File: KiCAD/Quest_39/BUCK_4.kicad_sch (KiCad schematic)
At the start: 21 parts

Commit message: Fixed most ERC errors
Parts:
- gave numbers to parts that had none: 21
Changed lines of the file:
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@@
   (symbol (lib_id "Device:C") (at 99.06 45.72 0) (unit 1)
     (in_bom yes) (on_board yes) (fields_autoplaced)
-    (property "Reference" "C?" (id 0) (at 102.87 44.4499 0)
+    (property "Reference" "C54" (id 0) (at 102.87 44.4499 0)
       (effects (font (size 1.27 1.27)) (justify left))
     )
@@
   (symbol (lib_id "Device:C_Polarized") (at 353.06 171.45 0) (unit 1)
     (in_bom yes) (on_board yes)
-    (property "Reference" "C?" (id 0) (at 356.8495 170.1375 0)
+    (property "Reference" "C60" (id 0) (at 356.8495 170.1375 0)
       (effects (font (size 1.27 1.27)) (justify left))
     )
@@
   (symbol (lib_id "Device:R") (at 321.31 214.63 0) (unit 1)
     (in_bom yes) (on_board yes) (fields_autoplaced)
-    (property "Reference" "R?" (id 0) (at 323.85 213.3599 0)
+    (property "Reference" "R27" (id 0) (at 323.85 213.3599 0)
       (effects (font (size 1.27 1.27)) (justify left))
     )
@@
   (symbol (lib_id "Device:C") (at 111.76 45.72 0) (unit 1)
     (in_bom yes) (on_board yes) (fields_autoplaced)
-    (property "Reference" "C?" (id 0) (at 115.57 44.4499 0)
+    (property "Reference" "C55" (id 0) (at 115.57 44.4499 0)
       (effects (font (size 1.27 1.27)) (justify left))
     )
@@
   (symbol (lib_id "Device:C_Polarized") (at 392.43 171.45 0) (unit 1)
     (in_bom yes) (on_board yes)
-    (property "Reference" "C?" (id 0) (at 396.2195 170.1375 0)
+    (property "Reference" "C63" (id 0) (at 396.2195 170.1375 0)
       (effects (font (size 1.27 1.27)) (justify left))
     )
@@
   (symbol (lib_id "MCP4151:MCP4151-502E{slash}SN") (at 252.73 219.71 0) (unit 1)
     (in_bom yes) (on_board yes)
-    (property "Reference" "U?" (id 0) (at 311.15 213.36 0)
+    (property "Reference" "U19" (id 0) (at 311.15 213.36 0)
       (effects (font (size 1.524 1.524)))
     )
@@
   (symbol (lib_id "Device:C_Polarized") (at 85.09 45.72 0) (unit 1)
     (in_bom yes) (on_board yes) (fields_autoplaced)
-    (property "Reference" "C?" (id 0) (at 88.9 43.5609 0)
+    (property "Reference" "C53" (id 0) (at 88.9 43.5609 0)
       (effects (font (size 1.27 1.27)) (justify left))
     )
@@
   (symbol (lib_id "Device:C") (at 336.55 223.52 0) (unit 1)
     (in_bom yes) (on_board yes) (fields_autoplaced)
-    (property "Reference" "C?" (id 0) (at 340.36 222.2499 0)
+    (property "Reference" "C64" (id 0) (at 340.36 222.2499 0)
       (effects (font (size 1.27 1.27)) (justify left))
     )
@@
   (symbol (lib_id "Device:C") (at 124.46 45.72 0) (unit 1)
     (in_bom yes) (on_board yes) (fields_autoplaced)
-    (property "Reference" "C?" (id 0) (at 128.27 44.4499 0)
+    (property "Reference" "C56" (id 0) (at 128.27 44.4499 0)
       (effects (font (size 1.27 1.27)) (justify left))
     )
@@
   (symbol (lib_id "Analog_ADC:INA226") (at 77.47 72.39 0) (unit 1)
     (in_bom yes) (on_board yes)
-    (property "Reference" "U?" (id 0) (at 82.55 60.96 0)
+    (property "Reference" "U17" (id 0) (at 82.55 60.96 0)
       (effects (font (size 1.27 1.27)) (justify left))
     )
@@
   (symbol (lib_id "Device:R") (at 46.99 48.26 0) (unit 1)
     (in_bom yes) (on_board yes) (fields_autoplaced)
-    (property "Reference" "R?" (id 0) (at 49.53 46.9899 0)
+    (property "Reference" "R24" (id 0) (at 49.53 46.9899 0)
       (effects (font (size 1.27 1.27)) (justify left))
     )
@@
   (symbol (lib_id "LTM4611EV:LTM4611EV-PBF") (at 130.81 101.6 0) (unit 1)
     (in_bom yes) (on_board yes)
-    (property "Reference" "U?" (id 0) (at 307.34 49.53 0)
+    (property "Reference" "U18" (id 0) (at 307.34 49.53 0)
       (effects (font (size 1.524 1.524)))
     )
@@
   (symbol (lib_id "Device:R") (at 125.73 90.17 0) (unit 1)
     (in_bom yes) (on_board yes) (fields_autoplaced)
-    (property "Reference" "R?" (id 0) (at 128.27 88.8999 0)
+    (property "Reference" "R26" (id 0) (at 128.27 88.8999 0)
       (effects (font (size 1.27 1.27)) (justify left))
     )
@@
   (symbol (lib_id "Device:R") (at 59.69 48.26 0) (unit 1)
     (in_bom yes) (on_board yes) (fields_autoplaced)
-    (property "Reference" "R?" (id 0) (at 62.23 46.9899 0)
+    (property "Reference" "R25" (id 0) (at 62.23 46.9899 0)
       (effects (font (size 1.27 1.27)) (justify left))
     )
@@
   (symbol (lib_id "Device:C_Polarized") (at 367.03 171.45 0) (unit 1)
     (in_bom yes) (on_board yes)
-    (property "Reference" "C?" (id 0) (at 370.8195 170.1375 0)
+    (property "Reference" "C61" (id 0) (at 370.8195 170.1375 0)
       (effects (font (size 1.27 1.27)) (justify left))
     )
@@
   (symbol (lib_id "Device:R") (at 54.61 40.64 90) (unit 1)
     (in_bom yes) (on_board yes) (fields_autoplaced)
-    (property "Reference" "R?" (id 0) (at 54.61 34.29 90))
+    (property "Reference" "R23" (id 0) (at 54.61 34.29 90))
     (property "Value" "0R0025" (id 1) (at 54.61 36.83 90))
     (property "Footprint" "" (id 2) (at 54.61 42.418 90)
@@
   (symbol (lib_id "Amplifier_Operational:MCP601-xOT") (at 34.29 64.77 0) (unit 1)
     (in_bom yes) (on_board yes)
-    (property "Reference" "U?" (id 0) (at 36.83 60.96 0))
+    (property "Reference" "U16" (id 0) (at 36.83 60.96 0))
     (property "Value" "MCP601T-I/OT" (id 1) (at 40.64 68.58 0))
     (property "Footprint" "Package_TO_SOT_SMD:SOT-23-5" (id 2) (at 31.75 69.85 0)
@@
   (symbol (lib_id "Device:C") (at 334.01 171.45 0) (unit 1)
     (in_bom yes) (on_board yes) (fields_autoplaced)
-    (property "Reference" "C?" (id 0) (at 337.82 170.1799 0)
+    (property "Reference" "C59" (id 0) (at 337.82 170.1799 0)
       (effects (font (size 1.27 1.27)) (justify left))
     )
@@
   (symbol (lib_id "Device:C") (at 54.61 54.61 90) (unit 1)
     (in_bom yes) (on_board yes)
-    (property "Reference" "C?" (id 0) (at 54.61 50.8 90))
+    (property "Reference" "C57" (id 0) (at 54.61 50.8 90))
     (property "Value" "1uF" (id 1) (at 54.61 58.42 90))
     (property "Footprint" "OptoDevice:R_LDR_4.9x4.2mm_P2.54mm_Vertical" (id 2) (at 58.42 53.6448 0)
@@
   (symbol (lib_id "Device:C_Polarized") (at 379.73 171.45 0) (unit 1)
     (in_bom yes) (on_board yes)
-    (property "Reference" "C?" (id 0) (at 383.5195 170.1375 0)
+    (property "Reference" "C62" (id 0) (at 383.5195 170.1375 0)
       (effects (font (size 1.27 1.27)) (justify left))
     )
@@
   (symbol (lib_id "Device:C") (at 127 135.89 0) (unit 1)
     (in_bom yes) (on_board yes) (fields_autoplaced)
-    (property "Reference" "C?" (id 0) (at 130.81 134.6199 0)
-      (effects (font (size 1.27 1.27)) (justify left))
-    )
+    (property "Reference" "C58" (id 0) (at 130.81 134.6199 0)
+      (effects (font (size 1.27 1.27)) (justify left))
+    )

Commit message: Gave all INA226's unique addresses
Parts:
- removed C53: 330uF, symbol Device:C_Polarized
- removed C54, C55, C56: 22uF, symbol Device:C
- removed C60, C61, C62, C63: 100uF, symbol Device:C_Polarized
- removed C64: 100nF, symbol Device:C
- removed R23: 0R0025, symbol Device:R
- removed R24, R25: 10, symbol Device:R
- removed R26: 10K, symbol Device:R
- removed R27: 20K, symbol Device:R
- removed U16: MCP601T-I/OT, Package_TO_SOT_SMD:SOT-23-5, symbol Amplifier_Operational:MCP601-xOT
- added C56: 330uF, symbol Device:C_Polarized
- added C60: 1uF, OptoDevice:R_LDR_4.9x4.2mm_P2.54mm_Vertical, symbol Device:C
- added C61, C62, C69: 100nF, symbol Device:C
- added C63: 10nF, symbol Device:C
- added C64, C65, C66, C67: 100uF, symbol Device:C_Polarized
- added C68: 100pF, symbol Device:C
- added R38: 0R0025, symbol Device:R
- added R39, R40: 10R, symbol Device:R
- added R41: 9k, symbol Device:R
- added R42: 1k, symbol Device:R
- added R43: 10k, symbol Device:R
- added R44: 20K, symbol Device:R
- added TP27, TP28, TP29, TP30, TP31, TP32, TP33: TestPoint, symbol Connector:TestPoint
- added U16: AD626ANZ, N_8_ADI, symbol AD626ANZ:AD626ANZ
- C57: value 1uF -> 22uF; footprint OptoDevice:R_LDR_4.9x4.2mm_P2.54mm_Vertical -> (none)
- C58: value 100nF -> 22uF
- C59: value 100pF -> 22uF
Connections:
- net +5V: now also U17.1 (A1), C62.1, C69.1, U16.6 (+VS)
- net GND: now also C61.2, C62.2, C69.2, U16.2 (AGND), U16.3 (-VS); no longer U17.1 (A1), U17.3 (~{Alert})
- net NEG: now also C57.2, C59.2, C56.2, C63.1, C64.2, C65.2, C66.2, C67.2, R42.2, U16.1 (-IN); no longer U17.8 (Vbus)
- net P0A: now also R44.2
- net POS: now also C64.1, C65.1, C66.1, C67.1, C68.1; no longer C59.1
- net PV_POS: now also C57.1, C58.1, C59.1, U18.A1 (VIN), U18.A2 (VIN), U18.A3 (VIN), U18.A4 (VIN), U18.A5 (VIN), U18.A6 (VIN), U18.B1 (VIN), U18.B2 (VIN), U18.B3 (VIN), U18.B4 (VIN), U18.B5 (VIN), U18.B6 (VIN), U18.C1 (VIN), U18.C2 (VIN), U18.C3 (VIN), U18.C4 (VIN), U18.C5 (VIN), U18.C6 (VIN), C56.1, R38.1, R38.2, R39.1, R40.1, R41.1, R43.1
- net RUN: now also R43.2
- net TRACK/SS: now also C63.2; no longer C58.1
- net Vfb: now also C68.2, R44.1; no longer C59.2
- net Vin+: now also C60.1, R39.2; no longer C57.1
- net Vin-: now also U17.8 (Vbus), U17.9 (Vin-), C60.2, R40.2, TP28.1, U16.5 (OUT)
- net at U18.A11 (COMP): now also TP31.1
- net at U18.A7 (INTVCC): now also U18.D9 (INTVCC), TP27.1
- net at U18.B12 (PLLFLTR/FSET): now also TP30.1
- net at U18.F11 (PGOOD): now also U18.G12 (PGOOD), TP29.1
- net at U18.K12 (DIFFVOUT), U18.L12 (VOUT_LCL): now also TP32.1, TP33.1
- new net: C61.1, U16.4 (FILTER)
- new net +IN: R41.2, R42.1, U16.8 (+IN)
- no-connect marks 16 -> 12
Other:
- note added: "10:1 divider"
- note added: "Addr=0x44"
- note added: "Extra mounting"
- note added: "G=10"
- note added: "Output voltage is set by varying Rfb with a digipot. SPI = 00"
- note added: "the measured voltage is divided and then amplified by 10 as to simulate a follower. This is done to make use of the AD626 (low price and availability)."

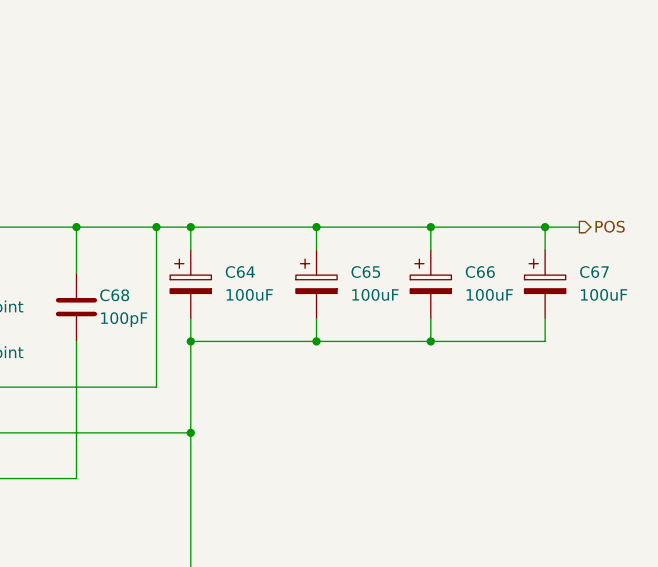
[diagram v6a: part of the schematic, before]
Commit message: Assigned all schem. symbols their footprints
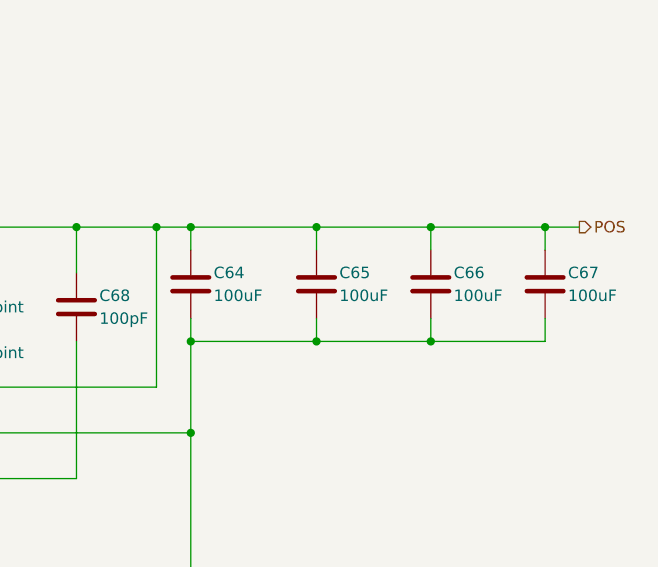
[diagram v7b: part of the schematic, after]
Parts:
- removed C64, C65, C66, C67: 100uF, symbol Device:C_Polarized
- added C64, C65, C66, C67: 100uF, Capacitor_SMD:C_1206_3216Metric, symbol Device:C
- C56: footprint (none) -> Capacitor_SMD:CP_Elec_8x6.9
- C57, C58, C59, C61, C62, C63, C68, C69: footprint (none) -> Capacitor_SMD:C_0805_2012Metric
- C60: footprint OptoDevice:R_LDR_4.9x4.2mm_P2.54mm_Vertical -> Capacitor_SMD:C_0805_2012Metric
- R38: footprint (none) -> Resistor_SMD:R_1206_3216Metric
- R39, R40, R41, R42, R43, R44: footprint (none) -> Resistor_SMD:R_0805_2012Metric
- TP27, TP28, TP29, TP30, TP31, TP32, TP33: footprint (none) -> TestPoint:TestPoint_Pad_D2.0mm
- U16: footprint N_8_ADI -> Package_DIP:DIP-8_W8.89mm_SMDSocket_LongPads
- U18: footprint LGA-133_3_LIT -> Package_LGA:Linear_LGA-133_15.0x15.0mm_Layout12x12_P1.27mm
- U19: footprint SOIC8-N_MC_MCH -> Package_SO:MSOP-8_3x3mm_P0.65mm
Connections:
- net NEG: now also C64.2, C65.2, C66.2, C67.2
- net POS: now also C64.1, C65.1, C66.1, C67.1

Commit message: Initial work on layout
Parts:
- C60, C61, C62, C63, C68, C69: footprint Capacitor_SMD:C_0805_2012Metric -> Capacitor_SMD:C_0603_1608Metric
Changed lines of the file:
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@@
       (effects (font (size 1.27 1.27)) (justify left))
     )
-    (property "Footprint" "Capacitor_SMD:C_0805_2012Metric" (id 2) (at 106.3752 127 0)
+    (property "Footprint" "Capacitor_SMD:C_0603_1608Metric" (id 2) (at 106.3752 127 0)
       (effects (font (size 1.27 1.27)) hide)
     )
@@
       (effects (font (size 1.27 1.27)) (justify left))
     )
-    (property "Footprint" "Capacitor_SMD:C_0805_2012Metric" (id 2) (at 26.3652 83.82 0)
+    (property "Footprint" "Capacitor_SMD:C_0603_1608Metric" (id 2) (at 26.3652 83.82 0)
       (effects (font (size 1.27 1.27)) hide)
     )
@@
       (effects (font (size 1.27 1.27)) (justify left))
     )
-    (property "Footprint" "Capacitor_SMD:C_0805_2012Metric" (id 2) (at 341.3252 223.52 0)
+    (property "Footprint" "Capacitor_SMD:C_0603_1608Metric" (id 2) (at 341.3252 223.52 0)
       (effects (font (size 1.27 1.27)) hide)
     )
@@
       (effects (font (size 1.27 1.27)) (justify left))
     )
-    (property "Footprint" "Capacitor_SMD:C_0805_2012Metric" (id 2) (at 64.4652 85.09 0)
+    (property "Footprint" "Capacitor_SMD:C_0603_1608Metric" (id 2) (at 64.4652 85.09 0)
       (effects (font (size 1.27 1.27)) hide)
     )
@@
       (effects (font (size 1.27 1.27)) (justify left))
     )
-    (property "Footprint" "Capacitor_SMD:C_0805_2012Metric" (id 2) (at 345.1352 171.45 0)
+    (property "Footprint" "Capacitor_SMD:C_0603_1608Metric" (id 2) (at 345.1352 171.45 0)
       (effects (font (size 1.27 1.27)) hide)
     )
@@
     (property "Reference" "C60" (id 0) (at 74.93 59.69 90))
     (property "Value" "1uF" (id 1) (at 74.93 67.31 90))
-    (property "Footprint" "Capacitor_SMD:C_0805_2012Metric" (id 2) (at 78.74 62.5348 0)
-      (effects (font (size 1.27 1.27)) hide)
-    )
+    (property "Footprint" "Capacitor_SMD:C_0603_1608Metric" (id 2) (at 78.74 62.5348 0)
+      (effects (font (size 1.27 1.27)) hide)
+    )
